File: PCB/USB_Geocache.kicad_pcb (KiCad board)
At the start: 4 copper layers, 25.5 x 49 mm, 44 parts, among them P1 USB_Mini_B, P2 Battery, P3 SWD, P4 GPS, P5 Button, P7 Servo, Q1 Q_PMOS_DSG, Q2 Q_PMOS_DSG, SW1 SW_PUSH, U1 MCP73831, U2 ILI9341_LCD, U3 LPC11U24FBD48/301, U4 LM3670MF, U5 EEPROM_SPI, X1 CRYSTAL_SMD

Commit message: Initial PCB layout
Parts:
- removed Q2: Q_PMOS_DSG, TO_SOT_Packages_SMD:SOT-23
- removed R12, R13: R, Resistors_SMD:R_0805
- removed R8: 4K7, Resistors_SMD:R_0805
- removed R9: ?, Resistors_SMD:R_0805
- removed SW1: SW_PUSH, Resistors_SMD:R_1210
- added D1: D, Diodes_SMD:SOD-123, F.Cu at (165.5, 70.0)
- added JP1: Jumper_NO_Small, Capacitors_SMD:C_0805, F.Cu at (149.5, 78.2)
- added Q3: Q_PMOS_DSG, TO_SOT_Packages_SMD:SOT-23, B.Cu at (155.0, 93.5)
- added R11: 10K, Resistors_SMD:R_0805_HandSoldering, B.Cu at (168.2, 69.8)
- C1, C10, C11, C12, C13, C16, C2, C4, C5, C6, C8: footprint Capacitors_SMD:C_0805 -> Capacitors_SMD:C_0805_HandSoldering
- C3: footprint Capacitors_SMD:C_0805 -> Capacitors_SMD:C_0805_HandSoldering; moved to F.Cu
- C7, C9: footprint Capacitors_SMD:C_0805 -> Capacitors_SMD:C_0805_HandSoldering; moved to B.Cu
- D2, D3: value DIODE -> D
- L1: footprint Resistors_SMD:R_1210 -> Resistors_SMD:R_1210_HandSoldering
- P2: footprint Connectors_JST:Connector_JST_PH-S2B -> Connectors_JST:JST_PH_S02B-PH-K-S_02x2.00mm_Angled
- P4: footprint Connectors_JST:Connector_JST_PH-S4B -> Connectors_JST:JST_PH_S04B-PH-K-S_04x2.00mm_Angled
- P5: footprint Connectors_JST:Connector_JST_PH-S2B -> Pin_Headers:Pin_Header_Straight_1x02
- R1, R2, R3, R7: footprint Resistors_SMD:R_0805 -> Resistors_SMD:R_0805_HandSoldering
- R10: value 2K2 -> 10K; footprint Resistors_SMD:R_0805 -> Resistors_SMD:R_0805_HandSoldering; moved to B.Cu
- R4: footprint Resistors_SMD:R_0805 -> Resistors_SMD:R_0805_HandSoldering; moved to F.Cu
- R5: value 10K -> 0R; footprint Resistors_SMD:R_0805 -> Resistors_SMD:R_0805_HandSoldering; moved to F.Cu
- R6: value 10K -> 2K2; footprint Resistors_SMD:R_0805 -> Resistors_SMD:R_0805_HandSoldering
- U1: value MCP73831 -> MCP73831/OT
- U2: value ILI9341_LCD -> ILI9341_LCD_Breakout; moved to F.Cu
- U3: value LPC11U24FBD48/301 -> LPC11U24FBD48; moved to F.Cu
- U4: footprint Housings_SOT-23_SOT-143_TSOT-6:SOT-23-5 -> TO_SOT_Packages_SMD:SOT-23-5
- U5: value EEPROM_SPI -> 25LC640A-I/SN; moved to B.Cu
- X1: value CRYSTAL_SMD -> 12.000MHz; footprint Crystals_Oscillators_SMD:Crystal_SMD_5032 -> Components:crystal_SMD_5032
- moved R5 30.3 mm to (169.0, 95.0), turned to 90 degrees
- moved U2 19.9 mm to (172.0, 77.6)
- moved R10 18.9 mm to (168.0, 66.0), turned to 180 degrees
- moved C12 18.5 mm to (169.2, 78.8), turned to 90 degrees
- moved C6 14.3 mm to (161.8, 89.0), turned to 0 degrees
- moved R3 13.3 mm to (151.5, 90.2)
- moved C1 13.2 mm to (152.2, 84.5), turned to 270 degrees
- moved C2 13.1 mm to (150.5, 84.5), turned to 270 degrees
- moved C11 12.3 mm to (161.5, 79.8), turned to 180 degrees
- moved P4 11.5 mm to (154.5, 83.2), turned to 270 degrees
- moved X1 9.22 mm to (161.8, 84.2), turned to 90 degrees
- moved R4 9.06 mm to (165.2, 72.2)
- moved C3 8.84 mm to (169.0, 65.5), turned to 90 degrees
- moved Q1 8.74 mm to (155.0, 96.8), turned to 270 degrees
- moved P7 8.51 mm to (160.2, 98.0), turned to 180 degrees
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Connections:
- net /BOOT_MODE renamed Net-(JP1-Pad1)
- C10 pad 1: +3V3 -> GND
- C10 pad 2: GND -> +3V3
- P5 pad 1: +BATT -> Net-(P5-Pad1)
- Q1 pad 3: /SERVO_EN -> Net-(Q1-Pad3)
- R1 pad 1: /SERVO_EN -> Net-(Q1-Pad3)
- R10 pad 1: Net-(R10-Pad1) -> /Button
- R5 pad 1: /Button -> +3V3
- R5 pad 2: GND -> /LCD_LED
- R6 pad 1: /EN -> +BATT
- R6 pad 2: GND -> Net-(P5-Pad1)
- U3 pad 1: /SERVO_SIGNAL -> (no net)
- U3 pad 11: (no net) -> /GPS_RX
- U3 pad 12: (no net) -> /SERVO_EN
- U3 pad 13: /BATT_STAT -> (no net)
- U3 pad 21: (no net) -> /SERVO_SIGNAL
- U3 pad 23: (no net) -> /EEPROM_CS
- U3 pad 24: /Enable -> (no net)
- U3 pad 25: (no net) -> /SPI_SCK
- U3 pad 30: /EEPROM_CS -> (no net)
- U3 pad 31: /SPI_SCK -> (no net)
- U3 pad 32: /BATT_VOLTAGE -> /Button
- U3 pad 38: /LED_PWM -> /Enable
- U3 pad 40: (no net) -> /BATT_STAT
- U3 pad 46: /GPS_RX -> (no net)
- U3 pad 48: /SERVO_EN -> (no net)
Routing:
- net GND: track 208.7 -> 78.8 mm, vias 12 -> 6
- net +3V3: track 143.3 -> 83.0 mm
- net +5V: track 31.6 -> 60.0 mm, vias 1 -> 4
- net /LCD_LED: track 27.5 -> 4.30 mm, vias 1 -> 0
- net /LED_PWM: track 19.6 -> 0.00 mm, vias 2 -> 0
- net /Button: track 6.38 -> 25.6 mm, vias 0 -> 1
- net +BATT: track 58.7 -> 76.1 mm, vias 1 -> 2
- net /BATT_VOLTAGE: track 17.0 -> 0.00 mm, vias 2 -> 0
- net /EN: track 30.1 -> 15.6 mm, vias 2 -> 1
- net /SW_CLK: track 5.63 -> 17.6 mm, vias 1 -> 2
- net /SPI_MISO: track 14.9 -> 24.3 mm, vias 0 -> 1
- net /SPI_MOSI: track 20.9 -> 12.1 mm
- net Net-(Q1-Pad3): track 0.00 -> 6.80 mm
- net /SPI_SCK: track 18.4 -> 12.3 mm, vias 0 -> 1
- net /SW_DIO: track 4.18 -> 10.1 mm, vias 1 -> 0
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- added copper zone on PWR, net +3V3
- removed copper zone on PWR, net GND
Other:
- board text added: "+"
- board text added: "-"
- board text added: "GPS"
- board text added: "PWM"
- board text added: "RX"
- board text added: "Servo"
- board text added: "USB"
- board text added: "V+"
- board text added: "V-"
- board text removed: "+ -"
- board text removed: "PWR"
- board text removed: "SIG"

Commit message: Fixes to schematic
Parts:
- removed R5: 0R, Resistors_SMD:R_0805_HandSoldering
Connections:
- U2 pad 8: /LCD_LED -> +3V3
- U3 pad 25: /SPI_SCK -> (no net)
- U3 pad 31: (no net) -> /SPI_SCK
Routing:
- net /LCD_LED: track 4.30 -> 0.00 mm
- net /SPI_SCK: track 12.3 -> 14.8 mm
- net +3V3: track 83.0 -> 84.2 mm
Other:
- net class Default: trace_width 0.2032 -> 0.254
- rule trace_min: 0.2032 -> 0.254

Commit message: Released revision B of PCB
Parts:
- moved U2 2.92 mm to (172.0, 74.7)
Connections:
- P4 pad 4: (no net) -> /GPS_TX
- U3 pad 12: /SERVO_EN -> /GPS_TX
- U3 pad 13: (no net) -> /SERVO_EN
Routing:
- net /GPS_TX: track 0.00 -> 5.52 mm
- net /SPI_MISO: track 24.3 -> 19.6 mm
- net /LCD_RESET: track 6.98 -> 4.98 mm
- net /LCD_DC: track 8.59 -> 6.61 mm
- net +BATT: track 76.1 -> 77.3 mm
- net /SPI_SCK: track 14.8 -> 16.0 mm
- net +3V3: track 84.2 -> 85.3 mm
- net /SPI_MOSI: track 12.1 -> 11.2 mm, vias 0 -> 1
- net /SERVO_EN: track 9.68 -> 8.81 mm
- net /BATT_STAT: track 19.8 -> 20.6 mm
- net /Button: track 25.6 -> 25.1 mm
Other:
- net class Default: via_dia 0.889 -> 1.143
- rule via_min_size: 0.889 -> 1.143
- board text added: "Reverse Geocache rev B 02/16"

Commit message: Fixes to PCB
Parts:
- removed D1: D, Diodes_SMD:SOD-123
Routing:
- net /SW_CLK: track 17.7 -> 29.7 mm
- net +5V: track 60.1 -> 56.9 mm, vias 4 -> 3
- net /Button: track 25.1 -> 28.2 mm
- net /SERVO_EN: track 8.81 -> 10.5 mm
- net /BATT_STAT: track 20.6 -> 21.2 mm
- net +BATT: track 77.3 -> 76.8 mm

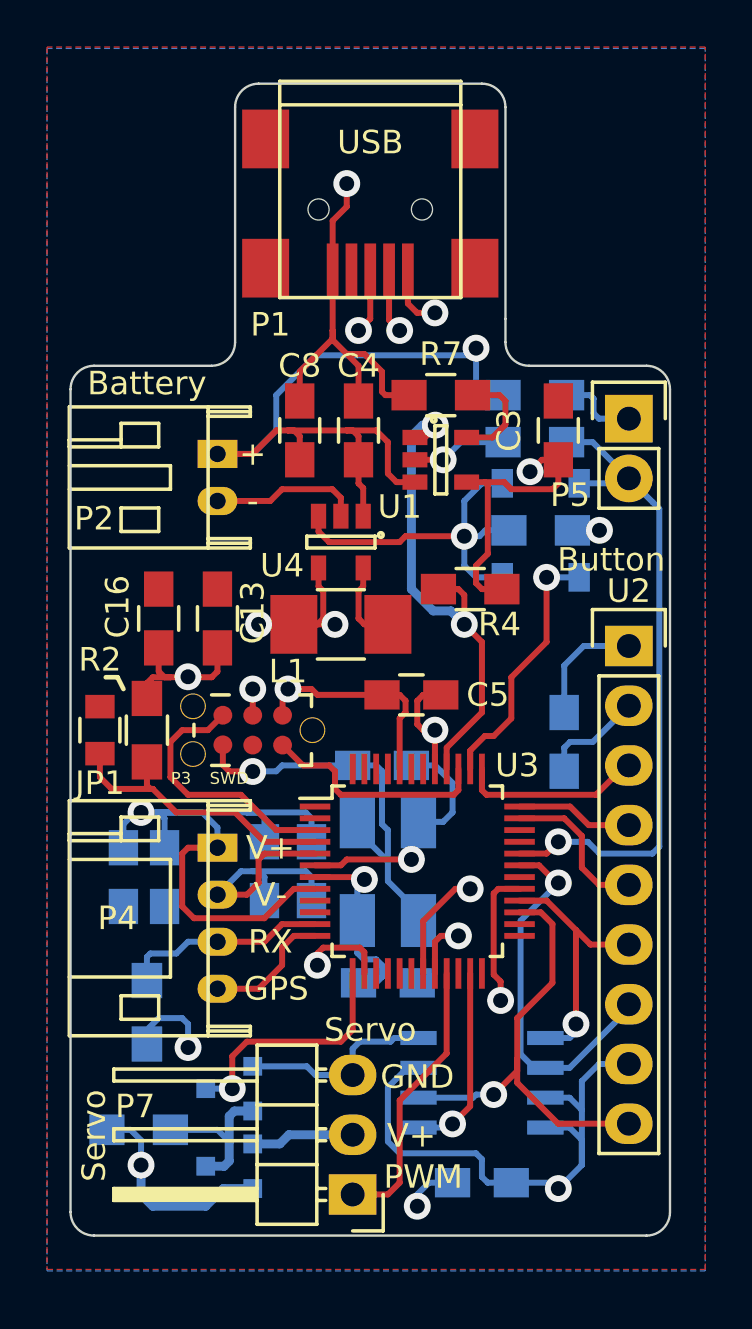
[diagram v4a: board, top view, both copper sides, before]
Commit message: Fixes to schematic and PCB layout
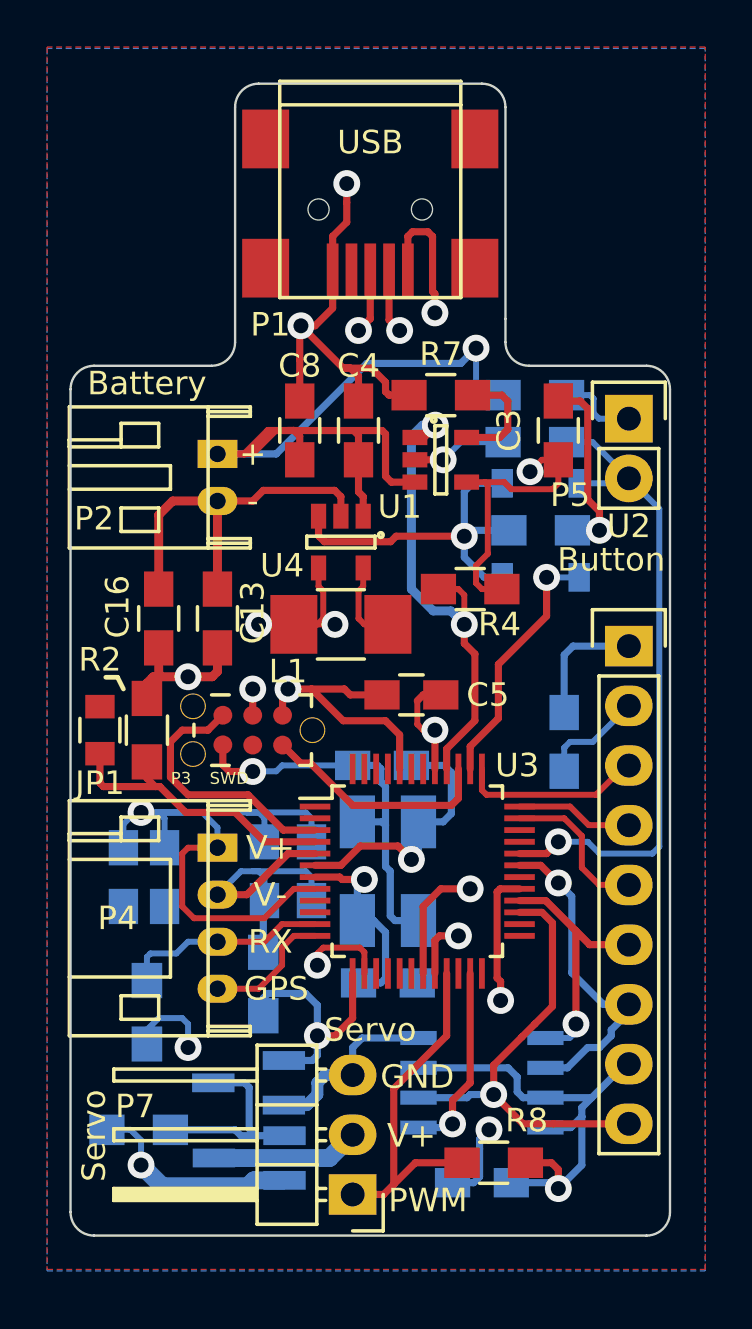
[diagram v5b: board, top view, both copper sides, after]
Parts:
- removed Q3: Q_PMOS_DSG, TO_SOT_Packages_SMD:SOT-23
- added Q2: DMP3098L, TO_SOT_Packages_SMD:SOT-23_Handsoldering, B.Cu at (155.8, 93.2)
- added R5: 4K7, Resistors_SMD:R_0805_HandSoldering, B.Cu at (156.4, 89.0)
- added R8: 4K7, Resistors_SMD:R_0805_HandSoldering, F.Cu at (166.2, 96.7)
- Q1: value Q_PMOS_DSG -> SSM3J328R; footprint TO_SOT_Packages_SMD:SOT-23 -> TO_SOT_Packages_SMD:SOT-23_Handsoldering
- R1: value R -> 4K7
- R6: value 2K2 -> 4K7
- moved Q1 0.92 mm to (155.8, 96.5)
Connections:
- Q1 pad 1: Net-(P7-Pad2) -> Net-(Q1-Pad1)
- Q1 pad 3: Net-(Q1-Pad3) -> Net-(P7-Pad2)
- R1 pad 1: Net-(Q1-Pad3) -> Net-(Q1-Pad1)
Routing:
- net +3V3: track 85.0 -> 168.2 mm
- net GND: track 78.6 -> 138.2 mm, vias 6 -> 7
- net Net-(Q1-Pad1): track 0.00 -> 8.74 mm
- net Net-(Q1-Pad3): track 6.80 -> 0.00 mm
- net +BATT: track 76.8 -> 82.4 mm
- net /SPI_MOSI: track 11.2 -> 16.5 mm
- net /SERVO_SIGNAL: track 11.9 -> 15.1 mm
- net +5V: track 56.9 -> 59.2 mm
- net Net-(P7-Pad2): track 4.41 -> 6.38 mm
- net /SPI_SCK: track 16.0 -> 14.7 mm
- net /XIN: track 10.8 -> 11.5 mm
- net /SW_CLK: track 29.7 -> 29.1 mm
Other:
- board text added: "Reverse Geocache rev B 03/16"
- board text removed: "Reverse Geocache rev B 02/16"

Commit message: Added current sense for the servo Added LED backlight FET for the LCD PCB improvements
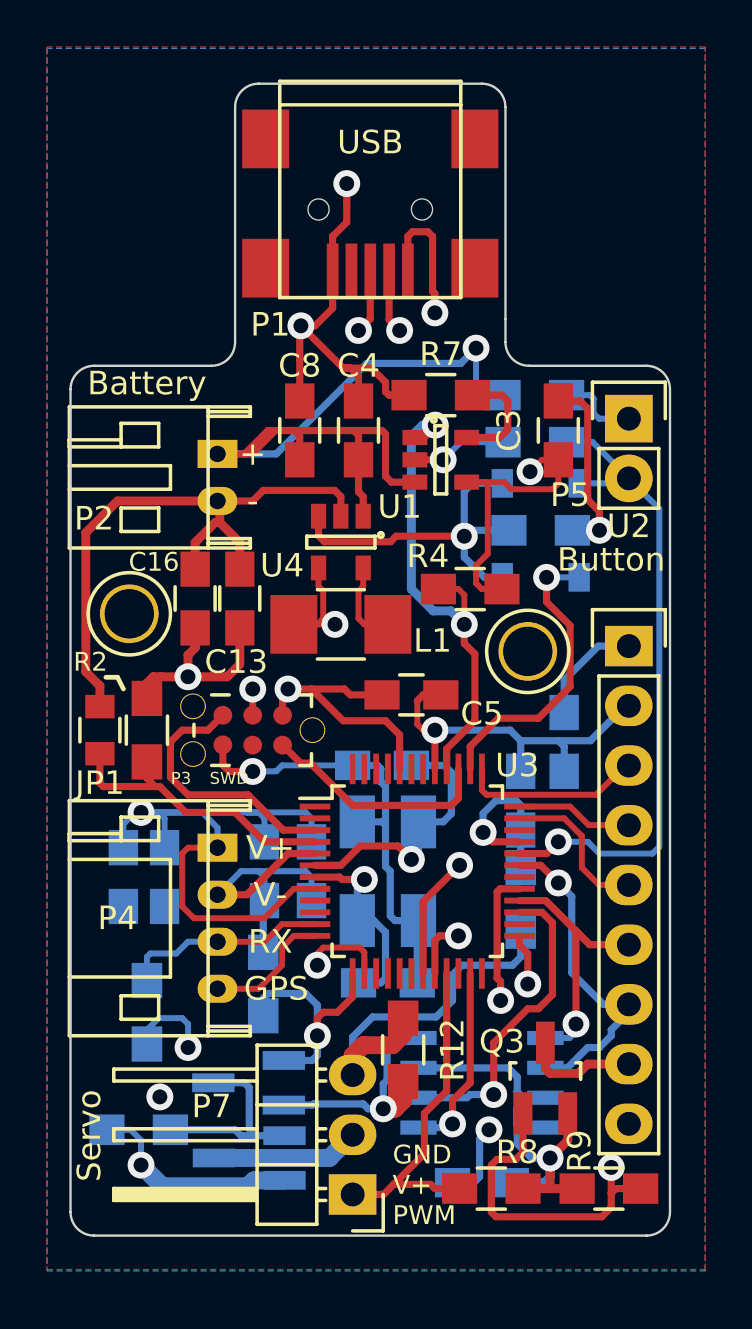
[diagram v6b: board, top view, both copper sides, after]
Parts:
- added C14: 10uF, Capacitors_SMD:C_0805_HandSoldering, B.Cu at (167.4, 81.2)
- added Q3: SSM3J328R, TO_SOT_Packages_SMD:SOT-23_Handsoldering, F.Cu at (168.4, 93.0)
- added R12: 0R1, Resistors_SMD:R_0805_HandSoldering, F.Cu at (162.4, 91.8)
- added R13: 10K, Resistors_SMD:R_0805_HandSoldering, B.Cu at (167.4, 85.5)
- added R9: 10K, Resistors_SMD:R_0805_HandSoldering, F.Cu at (171.2, 97.8)
- added REF**: MountingHole_2.1mm, Components:MountingHole2.1mm, F.Cu at (167.7, 74.9)
- added REF**: MountingHole_2.1mm, Components:MountingHole2.1mm, F.Cu at (150.8, 73.3)
- moved C16 1.77 mm to (153.6, 72.7)
- moved C13 1.27 mm to (155.4, 72.7)
- moved R8 1.10 mm to (166.2, 97.8)
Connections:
- P7 pad 3: GND -> /Rsense
- U2 pad 8: +3V3 -> Net-(Q3-Pad3)
- U3 pad 25: (no net) -> /BL
- U3 pad 33: (no net) -> /Vsense
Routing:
- net /BL: track 0.00 -> 31.5 mm, vias 0 -> 2
- net GND: track 138.2 -> 167.3 mm, vias 7 -> 9
- net /Rsense: track 0.00 -> 16.0 mm
- net +3V3: track 168.2 -> 159.5 mm, vias 7 -> 6
- net /Vsense: track 0.00 -> 7.08 mm, vias 0 -> 1
- net Net-(Q3-Pad3): track 0.00 -> 5.05 mm
- net /Enable: track 10.9 -> 12.7 mm
- net +5V: track 59.2 -> 60.8 mm
- net /D-: track 33.4 -> 32.3 mm
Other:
- board text added: "GND V+ PWM"
- board text added: "Reverse Geocache rev C 04/16"
- board text removed: "GND"
- board text removed: "PWM"
- board text removed: "Reverse Geocache rev B 03/16"

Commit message: Silkscreen improvements
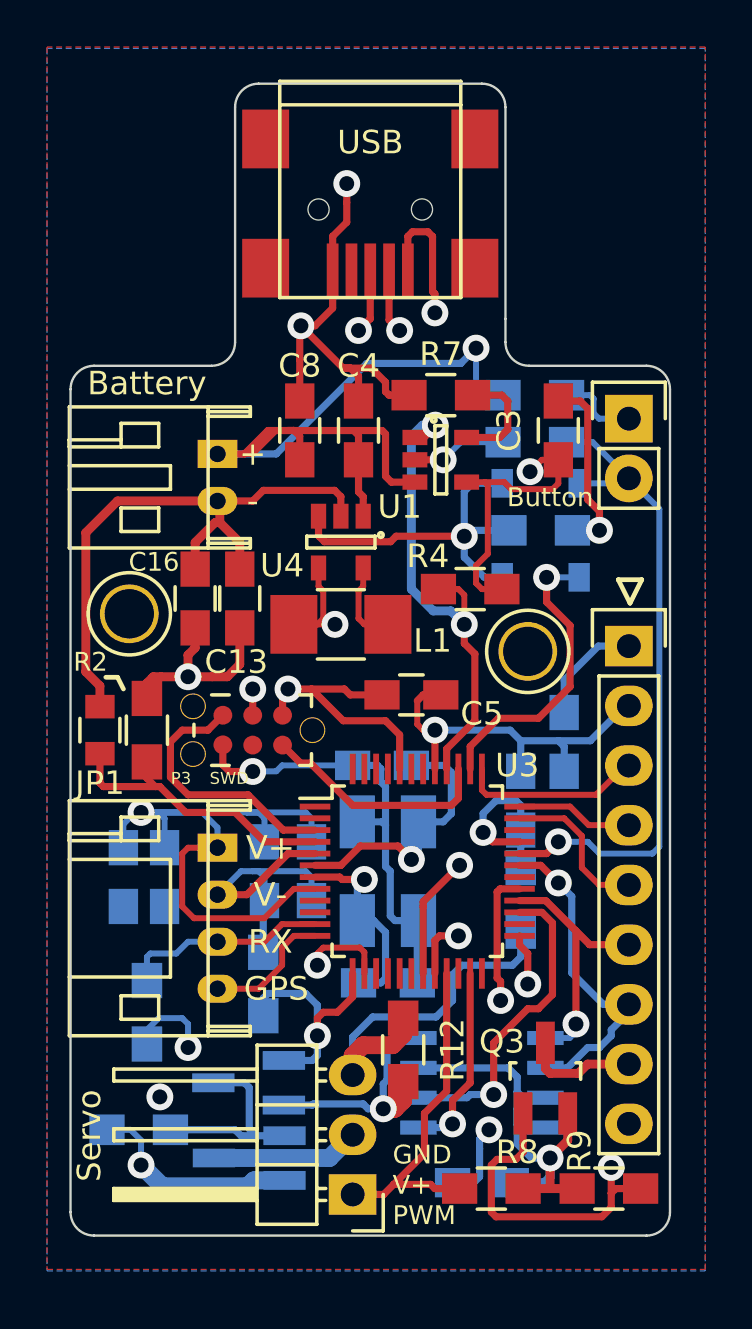
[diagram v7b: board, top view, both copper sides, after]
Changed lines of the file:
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@@
     (area 148.199999 50.699999 173.800001 99.800001)
     (thickness 1.6)
-    (drawings 31)
+    (drawings 34)
     (tracks 665)
     (zones 0)
@@
     (descr "Through hole pin header")
     (tags "pin header")
-    (fp_text reference P5 (at -2.5 3.25) (layer F.SilkS)
+    (fp_text reference P5 (at 2.75 -1.05) (layer F.SilkS) hide
       (effects (font (size 1 1) (thickness 0.15)))
     )
@@
     (descr "Through hole pin header")
     (tags "pin header")
-    (fp_text reference P7 (at 6 3.75 180) (layer F.SilkS)
+    (fp_text reference P7 (at 6 3.75 180) (layer F.SilkS) hide
       (effects (font (size 1 1) (thickness 0.15)))
     )
@@
     (tags "USB USB_B USB_Mini connector")
     (attr smd)
-    (fp_text reference P1 (at 5.75 4.25 360) (layer F.SilkS)
+    (fp_text reference P1 (at 5.75 4.25 360) (layer F.SilkS) hide
       (effects (font (size 1 1) (thickness 0.15)))
     )
@@
     (at 154.5 66.50076 270)
     (descr "JST PH series connector, JST_S02B-PH")
-    (fp_text reference P2 (at 2.74924 5.25 360) (layer F.SilkS)
+    (fp_text reference P2 (at 2.74924 5.25 360) (layer F.SilkS) hide
       (effects (font (size 1 1) (thickness 0.15)))
     )
@@
     (at 154.5 83.25 270)
     (descr "JST PH series connector, JST_S04B-PH")
-    (fp_text reference P4 (at 3 4.25 360) (layer F.SilkS)
+    (fp_text reference P4 (at 3 4.25 360) (layer F.SilkS) hide
       (effects (font (size 1 1) (thickness 0.15)))
     )
@@
     (descr "Through hole pin header")
     (tags "pin header")
-    (fp_text reference U2 (at 0 -5.1) (layer F.SilkS)
+    (fp_text reference U2 (at 2.85 -0.025) (layer F.SilkS) hide
       (effects (font (size 1 1) (thickness 0.15)))
     )
@@
     (pad 1 thru_hole circle (at 0 0) (size 2.5 2.5) (drill 2.1) (layers *.Cu *.Mask))
   )
+  (gr_line (start 171.55 71.85) (end 172.05 72.85) (layer F.SilkS) (width 0.2))
+  (gr_line (start 172.55 71.85) (end 171.55 71.85) (layer F.SilkS) (width 0.2))
+  (gr_line (start 172.05 72.85) (end 172.55 71.85) (layer F.SilkS) (width 0.2))
   (gr_text "Reverse \nGeocache\nrev C 04/16" (at 158.75 63.5 90) (layer B.SilkS)
     (effects (font (size 1 1) (thickness 0.15)) (justify left mirror))
   )
-  (gr_text Button (at 171.25 71) (layer F.SilkS)
-    (effects (font (size 1 1) (thickness 0.15)))
+  (gr_text Button (at 168.65 68.35) (layer F.SilkS)
+    (effects (font (size 0.8 0.8) (thickness 0.15)))
   )
   (gr_text USB (at 161 53.25) (layer F.SilkS)

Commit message: PCB updates
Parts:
- removed REF** (x2): MountingHole_2.1mm, Components:MountingHole2.1mm
- Q1, Q3: value SSM3J328R -> SI2301BDS-T1-E3
- Q2: value DMP3098L -> BST82
- R10, R11, R13, R2, R9: value 10K -> 4K7
- R7: value 2K -> 4K7
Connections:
- P3 pad 2: /SW_DIO -> /SW_CLK
- P3 pad 3: /SW_CLK -> (no net)
- P3 pad 4: (no net) -> Net-(P3-Pad4)
- U3 pad 1: (no net) -> Net-(U3-Pad1)
- U3 pad 10: (no net) -> Net-(U3-Pad10)
- U3 pad 15: (no net) -> Net-(U3-Pad15)
- U3 pad 16: (no net) -> Net-(U3-Pad16)
- U3 pad 17: (no net) -> Net-(U3-Pad17)
- U3 pad 18: (no net) -> Net-(U3-Pad18)
- U3 pad 2: (no net) -> Net-(U3-Pad2)
- U3 pad 22: (no net) -> Net-(U3-Pad22)
- U3 pad 24: (no net) -> Net-(U3-Pad24)
- U3 pad 26: (no net) -> Net-(U3-Pad26)
- U3 pad 30: (no net) -> Net-(U3-Pad30)
- U3 pad 34: (no net) -> Net-(U3-Pad34)
- U3 pad 39: /SW_DIO -> /SW_CLK
- U3 pad 42: (no net) -> Net-(U3-Pad42)
- U3 pad 43: (no net) -> Net-(U3-Pad43)
- U3 pad 45: (no net) -> Net-(U3-Pad45)
- U3 pad 46: (no net) -> Net-(U3-Pad46)
- U3 pad 47: (no net) -> Net-(U3-Pad47)
- U3 pad 48: (no net) -> Net-(U3-Pad48)
- U3 pad 9: (no net) -> Net-(U3-Pad9)
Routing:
- net /SW_DIO: track 9.92 -> 0.00 mm
- net /SW_CLK: track 29.1 -> 39.0 mm
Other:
- net class TestNet added: clearance 0.22, trace_width 0.35, via_dia 1.143, via_drill 0.635
